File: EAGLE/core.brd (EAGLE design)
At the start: 20.3 x 35.6 mm, 47 parts, among them IC1 MCP1825S-3302E, Q1 MMDT3904, U2 STM32F10XCXT6, U3 SST25VF040B-S2, X1 USB-MICROB, X2 IPEX-20279-001E, Y1 32Khz, Y2 8Mhz

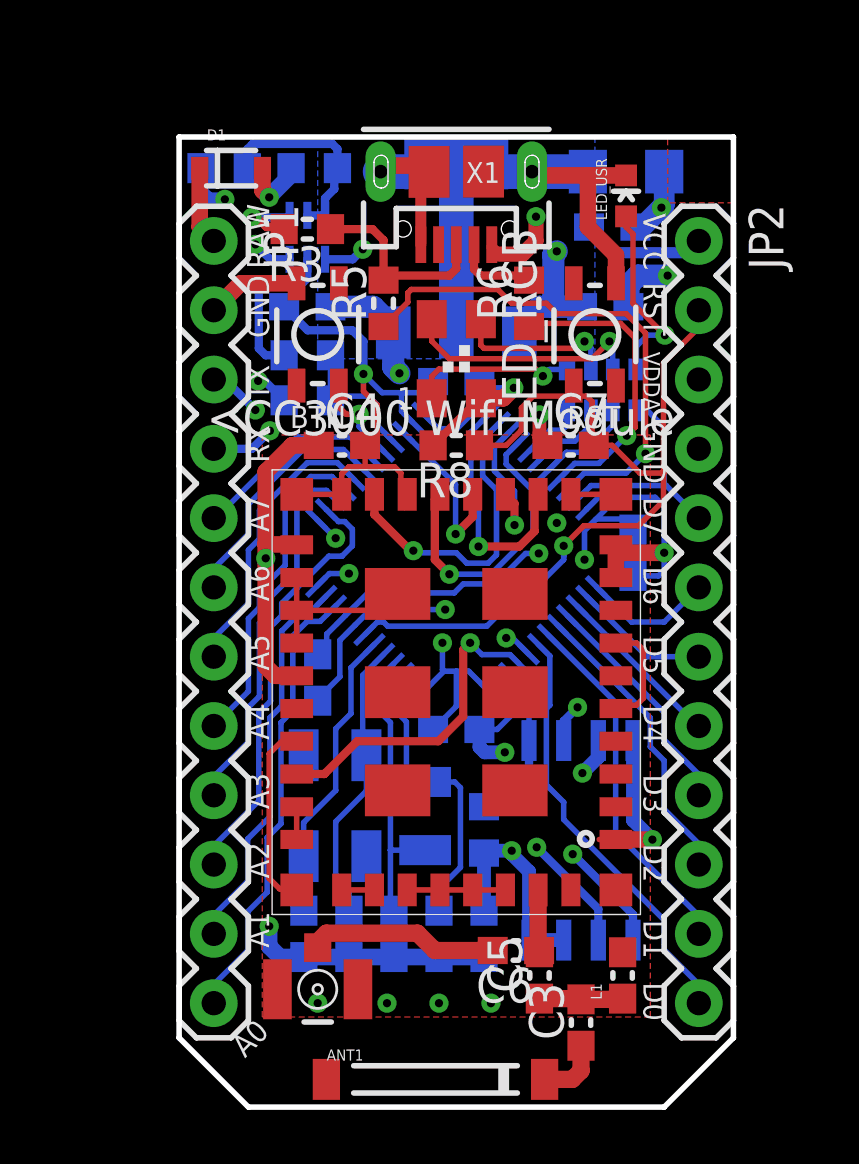
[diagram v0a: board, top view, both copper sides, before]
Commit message: Shifted Core board up and created mounting files
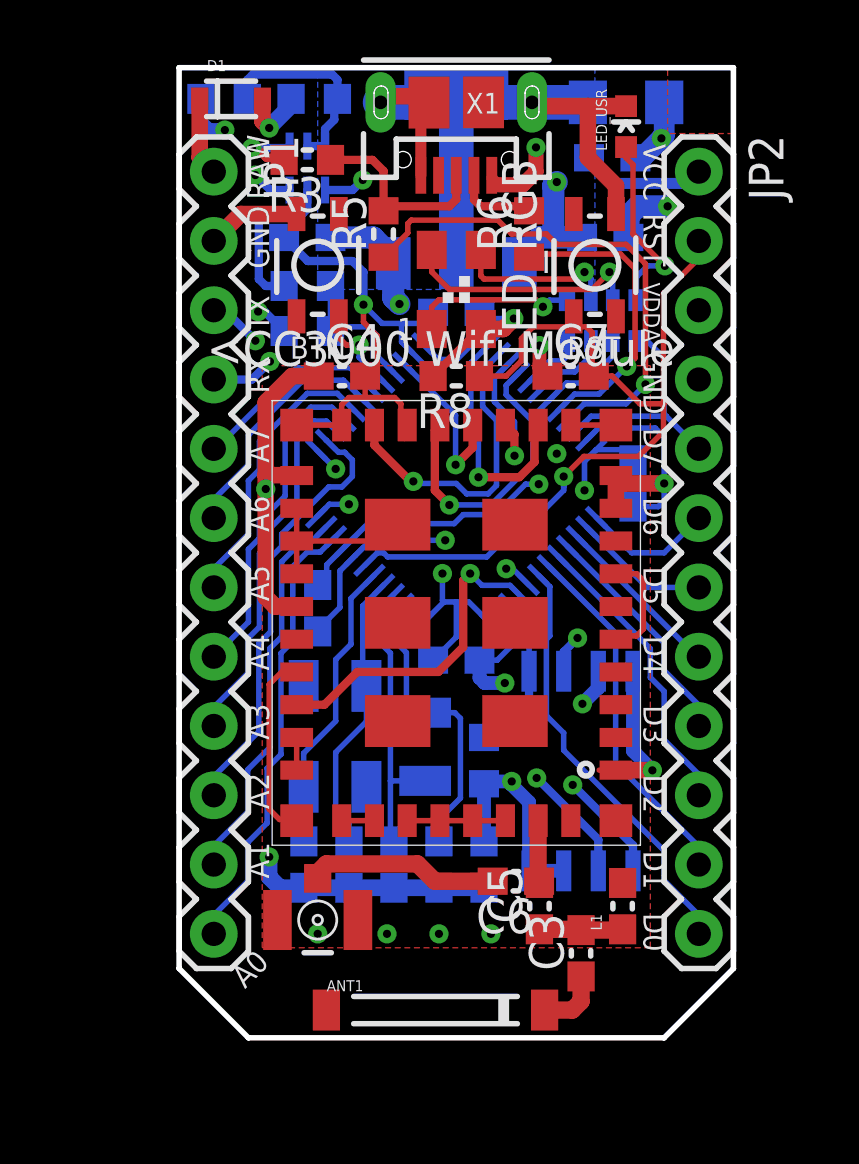
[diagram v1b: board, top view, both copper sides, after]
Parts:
- moved BTN 2.54 mm to (5.08, 28.3)
- moved C13 2.54 mm to (10.2, 26.6)
- moved C4 2.54 mm to (5.97, 24.3)
- moved C7 2.54 mm to (14.4, 24.3)
- moved D1 2.54 mm to (1.91, 34.4)
- moved L2 2.54 mm to (15.9, 32.3)
- moved LED_USR 2.54 mm to (16.4, 33.4)
- moved R1 2.54 mm to (4.95, 34.4)
- moved R2 2.54 mm to (1.65, 34.4)
- moved R3 2.54 mm to (4.70, 32.2)
- moved R4 2.54 mm to (4.70, 27.6)
- moved R7 2.54 mm to (4.70, 25.9)
- moved R8 2.54 mm to (10.2, 24.3)
- moved RESET 2.54 mm to (15.2, 28.3)
- moved RN1 2.54 mm to (15.5, 26.3)
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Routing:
- net VDDA: track 29.8 -> 35.1 mm
- net RAW: track 21.2 -> 25.7 mm
- net UVCC: track 15.6 -> 19.4 mm
- net TX: track 11.5 -> 15.4 mm
- net RX: track 8.26 -> 9.81 mm
- net SPI_SCK: track 28.8 -> 29.7 mm
- net SPI_MOSI: track 27.9 -> 28.6 mm
